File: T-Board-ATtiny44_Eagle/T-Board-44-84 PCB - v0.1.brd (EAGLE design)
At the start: 41.6 x 56.2 mm, 19 parts, among them IC1 LD11733TRS, IC4 NCP1117DT50GDT, J1 POWER_JACKPTH, J2 AVR_SPI_PRG_6PTH

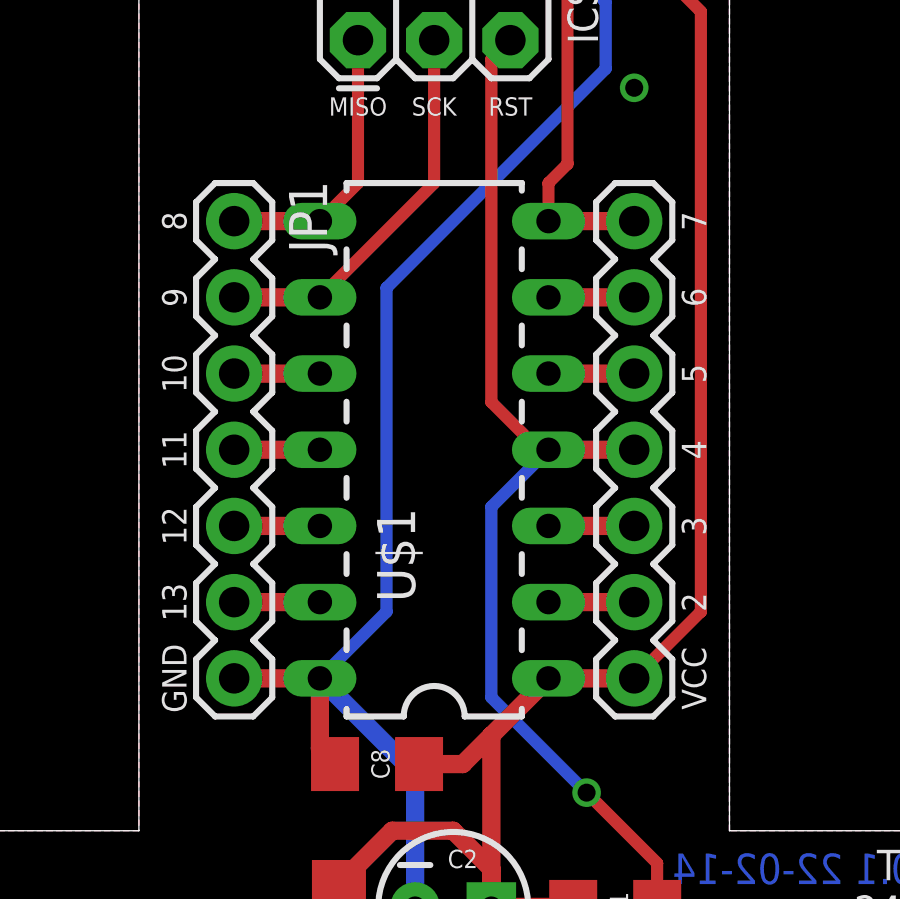
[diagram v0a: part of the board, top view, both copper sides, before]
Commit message: Adjusted header pins
Header pins spacing corrected to fit breadboard more precisely
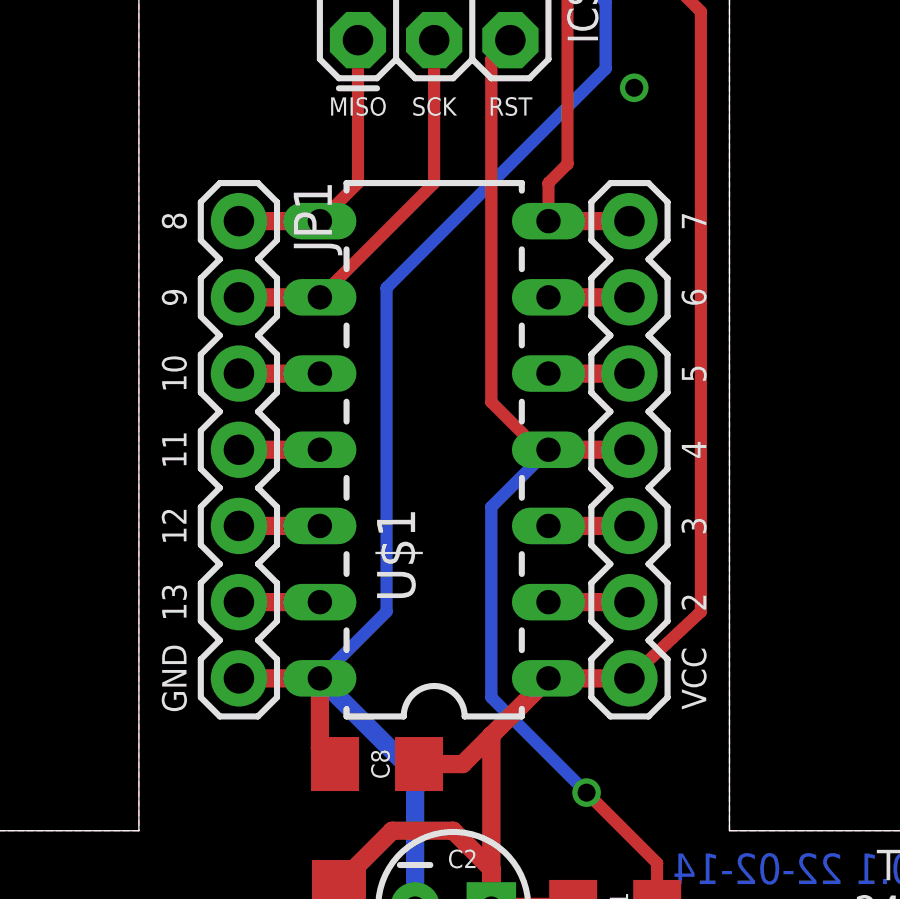
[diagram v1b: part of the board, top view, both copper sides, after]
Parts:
- moved JP1 0.16 mm to (20.2, 41.9)
- moved JP3 0.16 mm to (33.2, 26.7)
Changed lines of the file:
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@@
 <setting verticaltext="up"/>
 </settings>
-<grid distance="12.5" unitdist="mil" unit="mil" style="lines" multiple="1" display="yes" altdistance="12.5" altunitdist="mil" altunit="mil"/>
+<grid distance="0.15875" unitdist="mm" unit="mm" style="lines" multiple="1" display="yes" altdistance="0.15875" altunitdist="mm" altunit="mm"/>
 <layers>
 <layer number="1" name="Top" color="4" fill="1" visible="yes" active="yes"/>
@@
 <attribute name="VALUE" x="21.971" y="19.812" size="0.4064" layer="27" rot="R270"/>
 </element>
-<element name="JP3" library="SparkFun-Connectors" package="1X07" value="Pin 1-7" x="33.3375" y="26.67" smashed="yes" rot="R90">
-<attribute name="VALUE" x="36.5125" y="25.4" size="1.27" layer="27" rot="R90"/>
+<element name="JP3" library="SparkFun-Connectors" package="1X07" value="Pin 1-7" x="33.17875" y="26.67" smashed="yes" rot="R90">
+<attribute name="VALUE" x="36.35375" y="25.4" size="1.27" layer="27" rot="R90"/>
 </element>
 <element name="C8" library="SparkFun-Passives" package="1206" value="100nF" x="24.765" y="23.8125" smashed="yes">
@@
 <element name="S1" library="SparkFun-Electromechanical" package="TACTILE-PTH" value="" x="41.91" y="14.605" smashed="yes" rot="R180"/>
 <element name="LOGO1" library="SparkFun-Aesthetics" package="OSHW-LOGO-S" value="OSHW-LOGOS" x="34.6075" y="52.3875" rot="R90"/>
-<element name="JP1" library="SparkFun-Connectors" package="1X07" value="Pin 8-14" x="20.0025" y="41.91" rot="R270"/>
+<element name="JP1" library="SparkFun-Connectors" package="1X07" value="Pin 8-14" x="20.16125" y="41.91" rot="R270"/>
 <element name="U$1" library="SparkFun-DigitalIC" package="DIL14" value="ATTINY84ATTINY84-20PU" x="26.67" y="35.56" rot="R90"/>
 </elements>
@@
 <wire x1="39.0525" y1="3.175" x2="36.195" y2="3.175" width="0.6096" layer="16"/>
 <wire x1="10.16" y1="7.7" x2="13.16" y2="10.7" width="0.6096" layer="16"/>
-<wire x1="20.0025" y1="26.67" x2="22.86" y2="26.67" width="0.6096" layer="1"/>
+<wire x1="20.16125" y1="26.67" x2="22.86" y2="26.67" width="0.6096" layer="1"/>
 <wire x1="23.365" y1="23.8125" x2="22.86" y2="24.3175" width="0.6096" layer="1"/>
 <wire x1="22.86" y1="24.3175" x2="22.86" y2="26.67" width="0.6096" layer="1"/>
@@
 <wire x1="30.48" y1="26.67" x2="28.575" y2="24.765" width="0.6096" layer="1"/>
 <wire x1="28.575" y1="24.765" x2="28.575" y2="19.05" width="0.6096" layer="1"/>
-<wire x1="30.48" y1="26.67" x2="33.3375" y2="26.67" width="0.6096" layer="1"/>
+<wire x1="30.48" y1="26.67" x2="33.17875" y2="26.67" width="0.6096" layer="1"/>
 <wire x1="26.165" y1="23.8125" x2="27.6225" y2="23.8125" width="0.6096" layer="1"/>
 <wire x1="27.6225" y1="23.8125" x2="28.575" y2="24.765" width="0.6096" layer="1"/>
@@
 <wire x1="30.1625" y1="54.2925" x2="35.56" y2="48.895" width="0.4064" layer="1"/>
 <wire x1="35.56" y1="48.895" x2="35.56" y2="28.8925" width="0.4064" layer="1"/>
-<wire x1="35.56" y1="28.8925" x2="33.3375" y2="26.67" width="0.4064" layer="1"/>
+<wire x1="35.56" y1="28.8925" x2="33.17875" y2="26.67" width="0.4064" layer="1"/>
 </signal>
 <signal name="5V">
@@
 <contactref element="U$1" pad="9"/>
 <contactref element="JP1" pad="2"/>
-<wire x1="20.0025" y1="39.37" x2="22.86" y2="39.37" width="0.6096" layer="1"/>
+<wire x1="20.16125" y1="39.37" x2="22.86" y2="39.37" width="0.6096" layer="1"/>
 <wire x1="26.67" y1="47.9425" x2="26.67" y2="43.18" width="0.4064" layer="1"/>
 <wire x1="26.67" y1="43.18" x2="22.86" y2="39.37" width="0.4064" layer="1"/>
@@
 <contactref element="U$1" pad="8"/>
 <contactref element="JP1" pad="1"/>
-<wire x1="20.0025" y1="41.91" x2="22.86" y2="41.91" width="0.6096" layer="1"/>
+<wire x1="20.16125" y1="41.91" x2="22.86" y2="41.91" width="0.6096" layer="1"/>
 <wire x1="24.13" y1="47.9425" x2="24.13" y2="43.18" width="0.4064" layer="1"/>
 <wire x1="24.13" y1="43.18" x2="22.86" y2="41.91" width="0.4064" layer="1"/>
@@
 <contactref element="U$1" pad="7"/>
 <contactref element="JP3" pad="7"/>
-<wire x1="30.48" y1="41.91" x2="33.3375" y2="41.91" width="0.6096" layer="1"/>
+<wire x1="30.48" y1="41.91" x2="33.17875" y2="41.91" width="0.6096" layer="1"/>
 <wire x1="26.67" y1="50.4825" x2="26.67" y2="51.7525" width="0.4064" layer="1"/>
 <wire x1="26.67" y1="51.7525" x2="27.94" y2="53.0225" width="0.4064" layer="1"/>
@@
 <wire x1="34.1025" y1="19.05" x2="36.4744" y2="19.05" width="0.4064" layer="1"/>
 <wire x1="36.4744" y1="19.05" x2="38.6588" y2="16.8656" width="0.4064" layer="1"/>
-<wire x1="30.48" y1="34.29" x2="33.3375" y2="34.29" width="0.6096" layer="1"/>
+<wire x1="30.48" y1="34.29" x2="33.17875" y2="34.29" width="0.6096" layer="1"/>
 <wire x1="34.1025" y1="19.05" x2="34.1025" y2="20.5075" width="0.4064" layer="1"/>
 <wire x1="34.1025" y1="20.5075" x2="31.75" y2="22.86" width="0.4064" layer="1"/>
@@
 <contactref element="JP3" pad="5"/>
 <contactref element="U$1" pad="5"/>
-<wire x1="30.48" y1="36.83" x2="33.3375" y2="36.83" width="0.6096" layer="1"/>
+<wire x1="30.48" y1="36.83" x2="33.17875" y2="36.83" width="0.6096" layer="1"/>
 </signal>
 <signal name="N$8">
 <contactref element="JP3" pad="6"/>
 <contactref element="U$1" pad="6"/>
-<wire x1="30.48" y1="39.37" x2="33.3375" y2="39.37" width="0.6096" layer="1"/>
+<wire x1="30.48" y1="39.37" x2="33.17875" y2="39.37" width="0.6096" layer="1"/>
 </signal>
 <signal name="N$13">
 <contactref element="U$1" pad="10"/>
 <contactref element="JP1" pad="3"/>
-<wire x1="20.0025" y1="36.83" x2="22.86" y2="36.83" width="0.6096" layer="1"/>
+<wire x1="20.16125" y1="36.83" x2="22.86" y2="36.83" width="0.6096" layer="1"/>
 </signal>
 <signal name="N$14">
 <contactref element="U$1" pad="11"/>
 <contactref element="JP1" pad="4"/>
-<wire x1="20.0025" y1="34.29" x2="22.86" y2="34.29" width="0.6096" layer="1"/>
+<wire x1="20.16125" y1="34.29" x2="22.86" y2="34.29" width="0.6096" layer="1"/>
 </signal>
 <signal name="N$15">
 <contactref element="U$1" pad="12"/>
 <contactref element="JP1" pad="5"/>
-<wire x1="20.0025" y1="31.75" x2="22.86" y2="31.75" width="0.6096" layer="1"/>
+<wire x1="20.16125" y1="31.75" x2="22.86" y2="31.75" width="0.6096" layer="1"/>
 </signal>
 <signal name="N$16">
 <contactref element="U$1" pad="13"/>
 <contactref element="JP1" pad="6"/>
-<wire x1="20.0025" y1="29.21" x2="22.86" y2="29.21" width="0.6096" layer="1"/>
+<wire x1="20.16125" y1="29.21" x2="22.86" y2="29.21" width="0.6096" layer="1"/>
 </signal>
 <signal name="N$5">
 <contactref element="JP3" pad="2"/>
 <contactref element="U$1" pad="2"/>
-<wire x1="33.3375" y1="29.21" x2="30.48" y2="29.21" width="0.6096" layer="1"/>
+<wire x1="33.17875" y1="29.21" x2="30.48" y2="29.21" width="0.6096" layer="1"/>
 </signal>
 <signal name="N$6">
 <contactref element="JP3" pad="3"/>
 <contactref element="U$1" pad="3"/>
-<wire x1="30.48" y1="31.75" x2="33.3375" y2="31.75" width="0.6096" layer="1"/>
+<wire x1="30.48" y1="31.75" x2="33.17875" y2="31.75" width="0.6096" layer="1"/>
 </signal>
 </signals>
